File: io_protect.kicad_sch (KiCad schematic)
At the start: 27 parts, among them J201 RAILS IN, J202 CONTROL, J203 YOKE 1, J204 YOKE 2, U201 74LVC2G17, U202 74LVC2G17

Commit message: Schematic complete: all sheets wired, ERC clean, netlist verified, cap ratings set
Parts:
- C203, C204, C205, C206, C207, C208, C209, C210: Voltage (none) -> 25V
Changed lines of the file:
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@@
 			)
 		)
+		(property "Voltage" "25V"
+			(at 208.28 88.9 0)
+			(hide yes)
+			(show_name no)
+			(do_not_autoplace no)
+			(effects
+				(font
+					(size 1.27 1.27)
+				)
+			)
+		)
 		(pin "1"
 		)
@@
 			)
 		)
+		(property "Voltage" "25V"
+			(at 40.64 228.6 0)
+			(hide yes)
+			(show_name no)
+			(do_not_autoplace no)
+			(effects
+				(font
+					(size 1.27 1.27)
+				)
+			)
+		)
 		(pin "1"
 		)
@@
 			)
 		)
+		(property "Voltage" "25V"
+			(at 102.87 229.87 0)
+			(hide yes)
+			(show_name no)
+			(do_not_autoplace no)
+			(effects
+				(font
+					(size 1.27 1.27)
+				)
+			)
+		)
 		(pin "1"
 		)
@@
 			)
 		)
+		(property "Voltage" "25V"
+			(at 267.97 180.34 0)
+			(hide yes)
+			(show_name no)
+			(do_not_autoplace no)
+			(effects
+				(font
+					(size 1.27 1.27)
+				)
+			)
+		)
 		(pin "1"
 		)
@@
 			)
 		)
+		(property "Voltage" "25V"
+			(at 187.96 60.96 0)
+			(hide yes)
+			(show_name no)
+			(do_not_autoplace no)
+			(effects
+				(font
+					(size 1.27 1.27)
+				)
+			)
+		)
 		(pin "1"
 		)
@@
 			)
 		)
+		(property "Voltage" "25V"
+			(at 280.67 193.04 0)
+			(hide yes)
+			(show_name no)
+			(do_not_autoplace no)
+			(effects
+				(font
+					(size 1.27 1.27)
+				)
+			)
+		)
 		(pin "1"
 		)
@@
 			)
 		)
+		(property "Voltage" "25V"
+			(at 242.57 167.64 0)
+			(hide yes)
+			(show_name no)
+			(do_not_autoplace no)
+			(effects
+				(font
+					(size 1.27 1.27)
+				)
+			)
+		)
 		(pin "1"
 		)
@@
 			(at 293.37 193.04 0)
 			(hide yes)
+			(show_name no)
+			(do_not_autoplace no)
+			(effects
+				(font
+					(size 1.27 1.27)
+				)
+			)
+		)
+		(property "Voltage" "25V"
+			(at 293.37 193.04 0)
+			(hide yes)

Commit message: All footprints assigned; fuse moved to harness; project footprint library added
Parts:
- J201: footprint (none) -> Connector_Molex:Molex_Micro-Fit_3.0_43650-0400_1x04_P3.00mm_Horizontal; MPN (none) -> 43650-0400
- J202: footprint (none) -> Connector_Molex:Molex_Micro-Fit_3.0_43650-1200_1x12_P3.00mm_Horizontal; MPN (none) -> 43650-1200
- J203, J204: footprint (none) -> lev_lib:389690002
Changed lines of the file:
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@@
 			)
 		)
-		(property "Footprint" ""
+		(property "Footprint" "lev_lib:389690002"
 			(at 290.83 118.11 0)
 			(hide yes)
@@
 			)
 		)
-		(property "Footprint" ""
+		(property "Footprint" "Connector_Molex:Molex_Micro-Fit_3.0_43650-0400_1x04_P3.00mm_Horizontal"
 			(at 204.47 179.07 0)
 			(hide yes)
@@
 			)
 		)
+		(property "MPN" "43650-0400"
+			(at 204.47 179.07 0)
+			(hide yes)
+			(show_name no)
+			(do_not_autoplace no)
+			(effects
+				(font
+					(size 1.27 1.27)
+				)
+			)
+		)
 		(pin "3"
 		)
@@
 			)
 		)
-		(property "Footprint" ""
+		(property "Footprint" "lev_lib:389690002"
 			(at 290.83 105.41 0)
 			(hide yes)
@@
 			)
 		)
-		(property "Footprint" ""
+		(property "Footprint" "Connector_Molex:Molex_Micro-Fit_3.0_43650-1200_1x12_P3.00mm_Horizontal"
 			(at 69.85 63.5 0)
 			(hide yes)
@@
 			(at 69.85 63.5 0)
 			(hide yes)
+			(show_name no)
+			(do_not_autoplace no)
+			(effects
+				(font
+					(size 1.27 1.27)
+				)
+			)
+		)
+		(property "MPN" "43650-1200"
+			(at 69.85 63.5 0)
+			(hide yes)

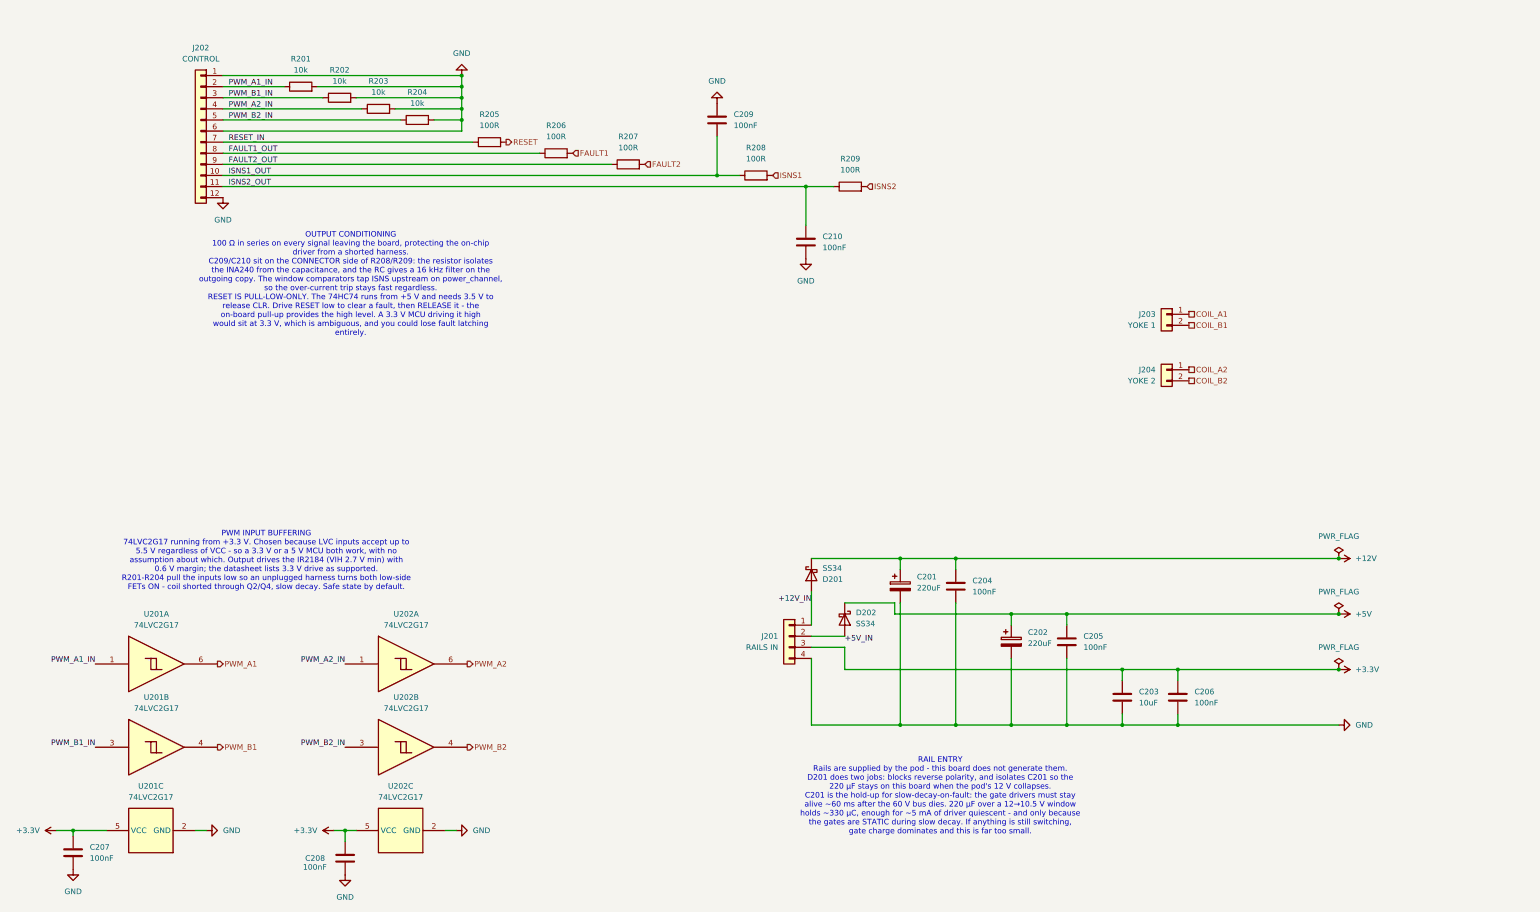
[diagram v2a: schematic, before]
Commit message: Adversarial review fixes: set-dominant latch, MCU enable, 3V3 hold-up, sense chain, 16-way connector
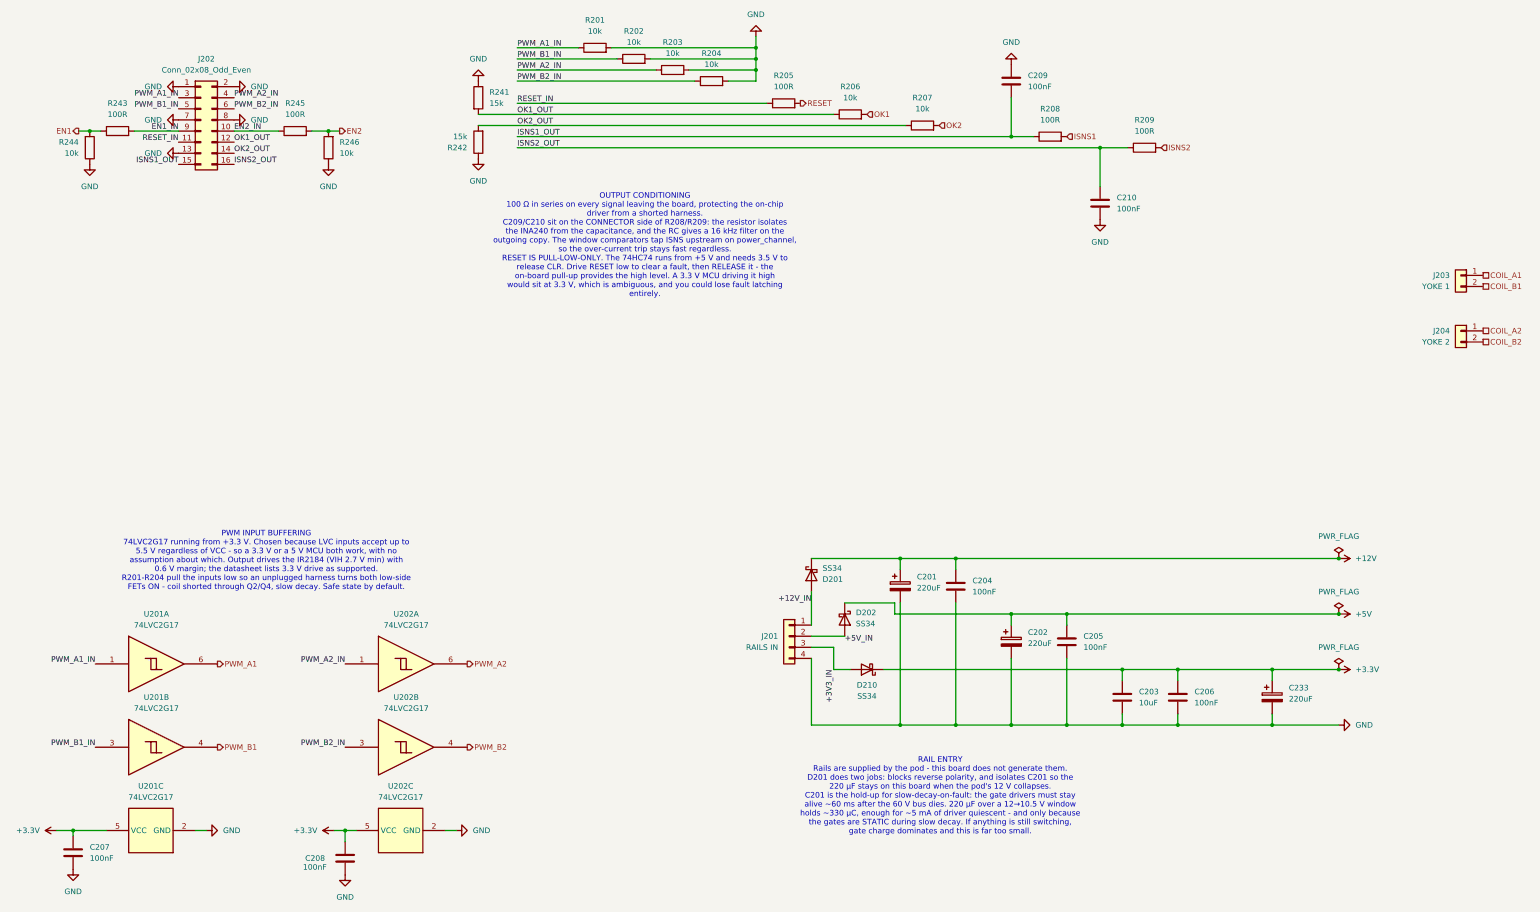
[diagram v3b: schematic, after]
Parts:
- removed J202: CONTROL, Connector_Molex:Molex_Micro-Fit_3.0_43650-1200_1x12_P3.00mm_Horizontal, symbol Connector_Generic:Conn_01x12
- added C233: 220uF, Capacitor_THT:CP_Radial_D8.0mm_P3.50mm, symbol Device:C_Polarized
- added D210: SS34, Diode_SMD:D_SMA_Handsoldering, symbol Device:D_Schottky
- added J202: Conn_02x08_Odd_Even, Connector_Molex:Molex_Micro-Fit_3.0_43045-1600_2x08_P3.00mm_Horizontal, symbol Connector_Generic:Conn_02x08_Odd_Even
- added R241, R242: 15k, Resistor_SMD:R_0805_2012Metric_Pad1.20x1.40mm_HandSolder, symbol Device:R
- added R243, R245: 100R, Resistor_SMD:R_0805_2012Metric_Pad1.20x1.40mm_HandSolder, symbol Device:R
- added R244, R246: 10k, Resistor_SMD:R_0805_2012Metric_Pad1.20x1.40mm_HandSolder, symbol Device:R
- R206, R207: value 100R -> 10k
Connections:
- net +3.3V: now also C233.1, D210.1 (K); no longer J201.3 (Pin_3)
- net GND: now also C233.2, J202.1 (Pin_1), J202.13 (Pin_13), J202.2 (Pin_2), J202.7 (Pin_7), J202.8 (Pin_8), R241.1, R242.1, R244.1, R246.1
- net ISNS1_OUT: now also J202.15 (Pin_15)
- net ISNS2_OUT: now also J202.16 (Pin_16)
- net PWM_A1_IN: now also J202.3 (Pin_3)
- net PWM_A2_IN: now also J202.4 (Pin_4)
- net PWM_B1_IN: now also J202.5 (Pin_5)
- net PWM_B2_IN: now also J202.6 (Pin_6)
- net RESET_IN: now also J202.11 (Pin_11)
- net FAULT1 renamed OK1
- net FAULT1_OUT renamed OK1_OUT
- net OK1_OUT: now also J202.12 (Pin_12), R241.2
- net FAULT2 renamed OK2
- net FAULT2_OUT renamed OK2_OUT
- net OK2_OUT: now also J202.14 (Pin_14), R242.2
- new net +3V3_IN: D210.2 (A), J201.3 (Pin_3)
- new net EN1: R243.1, R244.2
- new net EN1_IN: J202.9 (Pin_9), R243.2
- new net EN2: R245.2, R246.2
- new net EN2_IN: J202.10 (Pin_10), R245.1
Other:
- moved on the sheet: C209, C210, J203, J204, R201, R202, R203, R204, R205, R206, R207, R208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

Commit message: A14 modulation commitment (unipolar 3-level, 180 deg interleave); title blocks refreshed
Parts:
- J202: value Conn_02x08_Odd_Even -> CONTROL
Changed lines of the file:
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@@
 			)
 		)
-		(property "Value" "Conn_02x08_Odd_Even"
+		(property "Value" "CONTROL"
 			(at 71.12 49.53 0)
 			(show_name no)

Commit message: Delta review fixes: POR timing, comparator supply, trip point, SD divider, Schmitt gate
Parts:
- removed D210: SS34, Diode_SMD:D_SMA_Handsoldering, symbol Device:D_Schottky
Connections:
- net +3V3_IN is gone; now on net +3.3V: J201.3 (Pin_3)
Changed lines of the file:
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@@
 	(wire
 		(pts
-			(xy 214.63 186.69) (xy 218.44 186.69)
+			(xy 214.63 186.69) (xy 280.67 186.69)
 		)
 		(stroke
@@
 		(pts
 			(xy 229.87 161.29) (xy 229.87 163.83)
-		)
-		(stroke
-			(width 0)
-			(type default)
-		)
-	)
-	(wire
-		(pts
-			(xy 226.06 186.69) (xy 280.67 186.69)
 		)
 		(stroke
@@
 			)
 			(justify left bottom)
-		)
-	)
-	(label "+3V3_IN"
-		(at 214.63 186.69 270)
-		(effects
-			(font
-				(size 1.27 1.27)
-			)
-			(justify right bottom)
 		)
 	)
@@
 					(unit 1)
 				)
-			)
-		)
-	)
-	(symbol
-		(lib_id "Device:D_Schottky")
-		(at 222.25 186.69 180)
-		(unit 1)
-		(body_style 1)
-		(exclude_from_sim no)
-		(in_bom yes)
-		(on_board yes)
-		(in_pos_files yes)
-		(dnp no)
-		(property "Reference" "D210"
-			(at 222.25 190.246 0)
-			(show_name no)
-			(do_not_autoplace no)
-			(effects
-				(font
-					(size 1.27 1.27)
-				)
-			)
-		)
-		(property "Value" "SS34"
-			(at 222.25 192.786 0)
-			(show_name no)
-			(do_not_autoplace no)
-			(effects
-				(font
-					(size 1.27 1.27)
-				)
-			)
-		)
-		(property "Footprint" "Diode_SMD:D_SMA_Handsoldering"
-			(at 222.25 186.69 0)
-			(hide yes)
-			(show_name no)
-			(do_not_autoplace no)
-			(effects
-				(font
-					(size 1.27 1.27)
-				)
-			)
-		)
-		(property "Datasheet" ""
-			(at 222.25 186.69 0)
-			(hide yes)
-			(show_name no)
-			(do_not_autoplace no)
-			(effects
-				(font
-					(size 1.27 1.27)
-				)
-			)
-		)
-		(property "Description" "Schottky diode"
-			(at 222.25 186.69 0)
-			(hide yes)
-			(show_name no)
-			(do_not_autoplace no)
-			(effects
-				(font
-					(size 1.27 1.27)
-				)
-			)
-		)
-		(pin "2"
-		)
-		(pin "1"
-		)
-		(instances
-			(project "final_lev"
-				(path "/0a40c0f2-6b4c-4590-a920-c8cc820982d1/162916c8-3b57-4d49-9968-83d99e03257d"
-					(reference "D210")
-					(unit 1)
-				)

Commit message: Coil pours, test points, and a pad-rotation defect found by tooling
Board:

- 13 test points placed, grounds first so every signal point sits within 7.5 mm of its own ground return

- All four 30 A coil pours drawn on B.Cu, single polygons, 10.7-11.0 mm at the narrowest cut

- 34 vias transitioning the two A legs from the surface-mount shunts down to B.Cu, 15 at 2.0 A on CH1 and 19 at 1.58 A on CH2

- The B legs need no vias: every pad carrying their current is through-hole

Fixed:

- 20 footprints had pads that did not follow their body rotation, 5 of them off by 90 degrees, which turns a 1.175 x 1.450 mm pad across the part instead of along it. Repaired by Update Footprints from Library

- A12 corrected twice. The mounting holes are plated M3 pads on all four layers with no net, not the unplated holes I first reported

Tools:

- pour_check.py rasterises pour outlines at 0.05 mm; lay.py's bounding-box zone check was blind to polygons and missed a 6.5 mm band that needed 10.7

- lay.py gained pad-rotation and zone-priority checks, both regression tested against the broken versions
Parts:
- added TP209, TP210, TP211, TP212: TestPoint, TestPoint:TestPoint_Loop_D2.50mm_Drill1.0mm, symbol Connector:TestPoint
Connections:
- net +12V: now also TP209.1
- net +3.3V: now also TP211.1
- net +5V: now also TP210.1
- net GND: now also TP212.1
